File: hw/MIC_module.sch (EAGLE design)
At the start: 39 parts, among them J1 GROVE-4P-2.0-3470130P1, J2 GROVE-4P-2.0-3470130P1

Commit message: layout completed
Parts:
- removed J3: (no value), OPL-Connector:MICRO-SD-CARD-HOLDER-9P'MICROSD-9P'
- removed R6, R7, R9: 100k, rcl:R-EU_R0603
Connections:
- removed net SD_!CD: J3.CDN
- removed net SD_!CS: J3.CS, R9.1
- removed net SD_CLK: J3.SCLK
- removed net SD_MISO: J3.DO, R6.1
- removed net SD_MOSI: J3.DI, R7.1
- net +3V3: no longer J3.VDD, R6.2, R7.2, R9.2
- net GND: no longer J3.VSS
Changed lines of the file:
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@@
 <part name="C15" library="rcl" deviceset="C-EU" device="C0603" value="15p"/>
 <part name="GND27" library="supply1" deviceset="GND" device=""/>
-<part name="J3" library="OPL-Connector" deviceset="MICRO-SD-CARD-HOLDER-9P" device="'MICROSD-9P'"/>
-<part name="R6" library="rcl" deviceset="R-EU_" device="R0603" value="100k"/>
-<part name="R7" library="rcl" deviceset="R-EU_" device="R0603" value="100k"/>
-<part name="R9" library="rcl" deviceset="R-EU_" device="R0603" value="100k"/>
-<part name="+3V14" library="supply1" deviceset="+3V3" device=""/>
-<part name="GND28" library="supply1" deviceset="GND" device=""/>
 </parts>
 <sheets>
@@
 <instance part="C15" gate="G$1" x="195.58" y="149.86"/>
 <instance part="GND27" gate="1" x="195.58" y="142.24"/>
-<instance part="J3" gate="G$1" x="477.52" y="139.7"/>
-<instance part="R6" gate="G$1" x="452.12" y="157.48" rot="R90"/>
-<instance part="R7" gate="G$1" x="444.5" y="157.48" rot="R90"/>
-<instance part="R9" gate="G$1" x="436.88" y="157.48" rot="R90"/>
-<instance part="+3V14" gate="G$1" x="457.2" y="170.18"/>
-<instance part="GND28" gate="1" x="457.2" y="124.46"/>
 </instances>
 <busses>
@@
 <pinref part="C15" gate="G$1" pin="2"/>
 <pinref part="GND27" gate="1" pin="GND"/>
-</segment>
-<segment>
-<pinref part="J3" gate="G$1" pin="VSS"/>
-<wire x1="459.74" y1="137.16" x2="457.2" y2="137.16" width="0.1524" layer="91"/>
-<wire x1="457.2" y1="137.16" x2="457.2" y2="127" width="0.1524" layer="91"/>
-<pinref part="GND28" gate="1" pin="GND"/>
 </segment>
 </net>
@@
 <wire x1="180.34" y1="195.58" x2="180.34" y2="198.12" width="0.1524" layer="91"/>
 </segment>
-<segment>
-<pinref part="J3" gate="G$1" pin="VDD"/>
-<wire x1="459.74" y1="142.24" x2="457.2" y2="142.24" width="0.1524" layer="91"/>
-<wire x1="457.2" y1="142.24" x2="457.2" y2="165.1" width="0.1524" layer="91"/>
-<pinref part="+3V14" gate="G$1" pin="+3V3"/>
-<pinref part="R9" gate="G$1" pin="2"/>
-<wire x1="457.2" y1="165.1" x2="457.2" y2="167.64" width="0.1524" layer="91"/>
-<wire x1="457.2" y1="165.1" x2="452.12" y2="165.1" width="0.1524" layer="91"/>
-<wire x1="452.12" y1="165.1" x2="444.5" y2="165.1" width="0.1524" layer="91"/>
-<wire x1="444.5" y1="165.1" x2="436.88" y2="165.1" width="0.1524" layer="91"/>
-<wire x1="436.88" y1="165.1" x2="436.88" y2="162.56" width="0.1524" layer="91"/>
-<junction x="457.2" y="165.1"/>
-<pinref part="R7" gate="G$1" pin="2"/>
-<wire x1="444.5" y1="162.56" x2="444.5" y2="165.1" width="0.1524" layer="91"/>
-<junction x="444.5" y="165.1"/>
-<pinref part="R6" gate="G$1" pin="2"/>
-<wire x1="452.12" y1="162.56" x2="452.12" y2="165.1" width="0.1524" layer="91"/>
-<junction x="452.12" y="165.1"/>
-</segment>
 </net>
 <net name="JTMS" class="0">
@@
 </segment>
 </net>
-<net name="SD_!CS" class="0">
-<segment>
-<pinref part="J3" gate="G$1" pin="CS"/>
-<wire x1="459.74" y1="147.32" x2="436.88" y2="147.32" width="0.1524" layer="91"/>
-<pinref part="R9" gate="G$1" pin="1"/>
-<wire x1="436.88" y1="147.32" x2="431.8" y2="147.32" width="0.1524" layer="91"/>
-<wire x1="436.88" y1="152.4" x2="436.88" y2="147.32" width="0.1524" layer="91"/>
-<junction x="436.88" y="147.32"/>
-<label x="431.8" y="147.32" size="1.778" layer="95" rot="MR0"/>
-</segment>
-</net>
-<net name="SD_CLK" class="0">
-<segment>
-<pinref part="J3" gate="G$1" pin="SCLK"/>
-<wire x1="459.74" y1="139.7" x2="431.8" y2="139.7" width="0.1524" layer="91"/>
-<label x="431.8" y="139.7" size="1.778" layer="95" rot="MR0"/>
-</segment>
-</net>
-<net name="SD_MOSI" class="0">
-<segment>
-<pinref part="J3" gate="G$1" pin="DI"/>
-<wire x1="459.74" y1="144.78" x2="444.5" y2="144.78" width="0.1524" layer="91"/>
-<pinref part="R7" gate="G$1" pin="1"/>
-<wire x1="444.5" y1="144.78" x2="431.8" y2="144.78" width="0.1524" layer="91"/>
-<wire x1="444.5" y1="152.4" x2="444.5" y2="144.78" width="0.1524" layer="91"/>
-<junction x="444.5" y="144.78"/>
-<label x="431.8" y="144.78" size="1.778" layer="95" rot="MR0"/>
-</segment>
-</net>
-<net name="SD_MISO" class="0">
-<segment>
-<pinref part="J3" gate="G$1" pin="DO"/>
-<wire x1="459.74" y1="134.62" x2="452.12" y2="134.62" width="0.1524" layer="91"/>
-<pinref part="R6" gate="G$1" pin="1"/>
-<wire x1="452.12" y1="134.62" x2="431.8" y2="134.62" width="0.1524" layer="91"/>
-<wire x1="452.12" y1="152.4" x2="452.12" y2="134.62" width="0.1524" layer="91"/>
-<junction x="452.12" y="134.62"/>
-<label x="431.8" y="134.62" size="1.778" layer="95" rot="MR0"/>
-</segment>
-</net>
-<net name="SD_!CD" class="0">
-<segment>
-<pinref part="J3" gate="G$1" pin="CDN"/>
-<wire x1="459.74" y1="129.54" x2="431.8" y2="129.54" width="0.1524" layer="91"/>
-<label x="431.8" y="129.54" size="1.778" layer="95" rot="MR0"/>
-</segment>
-</net>

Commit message: layout in progress
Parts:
- removed U$6: STM32F303C, st:STM32F303C
- added C16, C18: 2u2, rcl:C-EUC0603
- added IC1: STM32F405RGT, micro-stm_v2:STM32F405RGT
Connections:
- removed net MIC_CLK_X2: U$6.PA5, U$6.PA6, U$6.PB13
- new net N$6: C16.2, IC1MCU.VCAP2
- new net N$9: C18.2, IC1MCU.VCAP1
- net +3V3: now also IC1MCU.VBAT, IC1MCU.VDDA, IC1PWR.VDD@1, IC1PWR.VDD@2, IC1PWR.VDD@3, IC1PWR.VDD@4; no longer U$6.VBAT, U$6.VDD_1, U$6.VDD_2, U$6.VDD_3, U$6.VDD_A
- net BOOT0: now also IC1MCU.BOOT0; no longer U$6.BOOT0
- net CAN_RX: now also IC1MCU.PB8; no longer U$6.PB8
- net CAN_TX: now also IC1MCU.PB9; no longer U$6.PB9
- net GND: now also C16.1, C18.1, IC1MCU.VSSA, IC1PWR.VSS@1, IC1PWR.VSS@2; no longer U$6.VSS_1, U$6.VSS_2, U$6.VSS_3, U$6.VSS_A
- net JTCK: now also IC1MCU.PA14; no longer U$6.PA14
- net JTDI: now also IC1MCU.PA15; no longer U$6.PA15
- net JTDO: now also IC1MCU.PB3; no longer U$6.PB3
- net JTMS: now also IC1MCU.PA13; no longer U$6.PA13
- net LED1: no longer U$6.PC13
- net MIC_CLK_UC: no longer U$6.PA2
- net MIC_PDM12: no longer U$6.PB15
- net MIC_PDM34: no longer U$6.PA7
- net NRST: now also IC1MCU.NRST; no longer U$6.NRST
- net OSC_IN: now also IC1MCU.OSC_IN; no longer U$6.PF0/OSC_IN

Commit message: added USB port
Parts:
- added J4: MICRO-USB-5P-340015001, OPL Eagle Library:MICRO-USB-5P-340015001
- added R11, R14: 22, rcl:R-EU_R0603
- added R6: 100k, rcl:R-EU_R0603
- added R8: 1k5, rcl:R-EU_R0603
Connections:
- new net N$3: J4.DM, R11.2
- new net N$32: J4.DP, R14.2, R8.2
- new net N$5: J4.ID, R6.2
- new net USB_N: IC1MCU.PA11, R11.1
- new net USB_P: IC1MCU.PA12, R14.1
- new net USB_VBUS: J4.VCC
- net +3V3: now also R8.1
- net GND: now also J4.GND@1, J4.GND@2, J4.GND@3, R6.1
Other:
- note added: "USB INTERFACE"
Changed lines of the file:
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@@
 <part name="GND32" library="supply1" deviceset="GND" device=""/>
 <part name="GND33" library="supply1" deviceset="GND" device=""/>
+<part name="GND38" library="supply1" deviceset="GND" device=""/>
+<part name="R11" library="rcl" deviceset="R-EU_" device="R0603" value="22"/>
+<part name="R14" library="rcl" deviceset="R-EU_" device="R0603" value="22"/>
+<part name="R6" library="rcl" deviceset="R-EU_" device="R0603" value="100k"/>
+<part name="GND35" library="supply1" deviceset="GND" device=""/>
+<part name="R8" library="rcl" deviceset="R-EU_" device="R0603" value="1k5"/>
+<part name="+3V15" library="supply1" deviceset="+3V3" device=""/>
+<part name="J4" library="OPL Eagle Library" deviceset="MICRO-USB-5P" device="-340015001"/>
 </parts>
 <sheets>
@@
 <wire x1="55.88" y1="5.08" x2="55.88" y2="43.18" width="0.1524" layer="94"/>
 <text x="58.42" y="38.1" size="2.54" layer="94">R2P BUS</text>
+<wire x1="152.4" y1="55.88" x2="213.36" y2="55.88" width="0.1524" layer="94"/>
+<wire x1="213.36" y1="55.88" x2="213.36" y2="5.08" width="0.1524" layer="94"/>
+<wire x1="213.36" y1="5.08" x2="152.4" y2="5.08" width="0.1524" layer="94"/>
+<wire x1="152.4" y1="5.08" x2="152.4" y2="55.88" width="0.1524" layer="94"/>
+<text x="154.94" y="50.8" size="2.54" layer="94">USB INTERFACE</text>
 </plain>
 <instances>
@@
 <instance part="GND32" gate="1" x="20.32" y="284.48"/>
 <instance part="GND33" gate="1" x="12.7" y="284.48"/>
+<instance part="GND38" gate="1" x="190.5" y="12.7"/>
+<instance part="R11" gate="G$1" x="172.72" y="33.02"/>
+<instance part="R14" gate="G$1" x="172.72" y="25.4"/>
+<instance part="R6" gate="G$1" x="182.88" y="20.32" rot="R90"/>
+<instance part="GND35" gate="1" x="182.88" y="12.7"/>
+<instance part="R8" gate="G$1" x="190.5" y="45.72" rot="R180"/>
+<instance part="+3V15" gate="G$1" x="198.12" y="53.34"/>
+<instance part="J4" gate="USB" x="200.66" y="27.94" rot="MR0"/>
 </instances>
 <busses>
@@
 <pinref part="C18" gate="G$1" pin="1"/>
 <pinref part="GND33" gate="1" pin="GND"/>
+</segment>
+<segment>
+<pinref part="GND38" gate="1" pin="GND"/>
+<wire x1="190.5" y1="15.24" x2="190.5" y2="22.86" width="0.1524" layer="91"/>
+<wire x1="200.66" y1="15.24" x2="198.12" y2="15.24" width="0.1524" layer="91"/>
+<wire x1="198.12" y1="15.24" x2="195.58" y2="15.24" width="0.1524" layer="91"/>
+<wire x1="195.58" y1="15.24" x2="193.04" y2="15.24" width="0.1524" layer="91"/>
+<wire x1="193.04" y1="15.24" x2="190.5" y2="15.24" width="0.1524" layer="91"/>
+<junction x="190.5" y="15.24"/>
+<pinref part="J4" gate="USB" pin="GND@1"/>
+<pinref part="J4" gate="USB" pin="GND@2"/>
+<wire x1="200.66" y1="15.24" x2="210.82" y2="15.24" width="0.1524" layer="91"/>
+<wire x1="210.82" y1="15.24" x2="210.82" y2="26.67" width="0.1524" layer="91"/>
+<pinref part="J4" gate="USB" pin="GND@3"/>
+<wire x1="210.82" y1="26.67" x2="210.82" y2="29.21" width="0.1524" layer="91"/>
+<junction x="210.82" y="26.67"/>
+</segment>
+<segment>
+<pinref part="R6" gate="G$1" pin="1"/>
+<pinref part="GND35" gate="1" pin="GND"/>
 </segment>
 </net>
@@
 <pinref part="+3V14" gate="G$1" pin="+3V3"/>
 </segment>
+<segment>
+<pinref part="R8" gate="G$1" pin="1"/>
+<wire x1="195.58" y1="45.72" x2="198.12" y2="45.72" width="0.1524" layer="91"/>
+<wire x1="198.12" y1="45.72" x2="198.12" y2="50.8" width="0.1524" layer="91"/>
+<pinref part="+3V15" gate="G$1" pin="+3V3"/>
+</segment>
 </net>
 <net name="JTMS" class="0">
@@
 </segment>
 </net>
+<net name="USB_VBUS" class="0">
+<segment>
+<wire x1="190.5" y1="33.02" x2="187.96" y2="33.02" width="0.1524" layer="91"/>
+<label x="170.18" y="40.64" size="1.778" layer="95" rot="MR0"/>
+<wire x1="187.96" y1="33.02" x2="187.96" y2="40.64" width="0.1524" layer="91"/>
+<wire x1="187.96" y1="40.64" x2="170.18" y2="40.64" width="0.1524" layer="91"/>
+<pinref part="J4" gate="USB" pin="VCC"/>
+</segment>
+</net>
+<net name="USB_N" class="0">
+<segment>
+<pinref part="R11" gate="G$1" pin="1"/>
+<wire x1="167.64" y1="33.02" x2="165.1" y2="33.02" width="0.1524" layer="91"/>
+<label x="165.1" y="33.02" size="1.778" layer="95" rot="MR0"/>
+</segment>
+<segment>
+<pinref part="IC1" gate="MCU" pin="PA11"/>
+<wire x1="68.58" y1="325.12" x2="71.12" y2="325.12" width="0.1524" layer="91"/>
+<label x="71.12" y="325.12" size="1.778" layer="95"/>
+</segment>
+</net>
+<net name="USB_P" class="0">
+<segment>
+<pinref part="R14" gate="G$1" pin="1"/>
+<wire x1="167.64" y1="25.4" x2="165.1" y2="25.4" width="0.1524" layer="91"/>
+<label x="165.1" y="25.4" size="1.778" layer="95" rot="MR0"/>
+</segment>
+<segment>
+<pinref part="IC1" gate="MCU" pin="PA12"/>
+<wire x1="68.58" y1="327.66" x2="71.12" y2="327.66" width="0.1524" layer="91"/>
+<label x="71.12" y="327.66" size="1.778" layer="95"/>
+</segment>
+</net>
+<net name="N$3" class="0">
+<segment>
+<wire x1="190.5" y1="30.48" x2="180.34" y2="30.48" width="0.1524" layer="91"/>
+<wire x1="180.34" y1="30.48" x2="180.34" y2="33.02" width="0.1524" layer="91"/>
+<pinref part="R11" gate="G$1" pin="2"/>
+<wire x1="180.34" y1="33.02" x2="177.8" y2="33.02" width="0.1524" layer="91"/>
+<pinref part="J4" gate="USB" pin="DM"/>
+</segment>
+</net>
+<net name="N$32" class="0">
+<segment>
+<wire x1="190.5" y1="27.94" x2="182.88" y2="27.94" width="0.1524" layer="91"/>
+<wire x1="182.88" y1="27.94" x2="180.34" y2="27.94" width="0.1524" layer="91"/>
+<wire x1="180.34" y1="27.94" x2="180.34" y2="25.4" width="0.1524" layer="91"/>
+<pinref part="R14" gate="G$1" pin="2"/>
+<wire x1="180.34" y1="25.4" x2="177.8" y2="25.4" width="0.1524" layer="91"/>
+<pinref part="R8" gate="G$1" pin="2"/>
+<wire x1="185.42" y1="45.72" x2="182.88" y2="45.72" width="0.1524" layer="91"/>
+<wire x1="182.88" y1="45.72" x2="182.88" y2="27.94" width="0.1524" layer="91"/>
+<junction x="182.88" y="27.94"/>
+<pinref part="J4" gate="USB" pin="DP"/>
+</segment>
+</net>
+<net name="N$5" class="0">
+<segment>
+<pinref part="R6" gate="G$1" pin="2"/>
+<wire x1="182.88" y1="25.4" x2="190.5" y2="25.4" width="0.1524" layer="91"/>
+<pinref part="J4" gate="USB" pin="ID"/>
+</segment>
+</net>

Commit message: layout completed
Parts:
- removed R3: 10k, rcl:R-EU_R0603
- added C19: 100n, rcl:C-EUC0603
- added X1: 53047-04, con-molex:53047-04
- added X2: 53047-06, con-molex:53047-06
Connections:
- removed net BOOT0: IC1MCU.BOOT0, R3.2
- new net I2C2_SCL: IC1MCU.PB10, X1-3.S
- new net I2C2_SDA: IC1MCU.PB11, X1-4.S
- new net I2S3_CK: IC1MCU.PC10, X2-4.S
- new net I2S3_MCK: IC1MCU.PC7, X2-5.S
- new net I2S3_SD: IC1MCU.PC12, X2-3.S
- new net I2S3_WS: IC1MCU.PA4, X2-6.S
- new net MIC_CLK_X2: IC1MCU.PA5, IC1MCU.PA6, IC1MCU.PB13
- net +3V3: now also C19.1, X1-1.S, X2-1.S
- net GND: now also C19.2, IC1MCU.BOOT0, LED1.C, X1-2.S, X2-2.S; no longer LED1.A, R3.1
- net LED1: now also IC1MCU.PB7
- net MIC_CLK_UC: now also IC1MCU.PB0
- net MIC_PDM12: now also IC1MCU.PB15
- net MIC_PDM34: now also IC1MCU.PA7
- net N$4: now also LED1.A; no longer LED1.C
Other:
- note added: "MIC ARRAY"
- moved on the sheet: C10, C11, C12, C13, C15, C16, C18, IC1, LED1, R2, R4, R5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

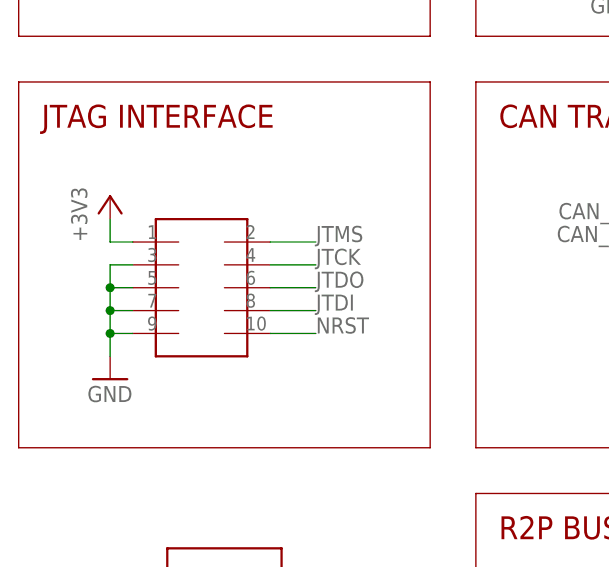
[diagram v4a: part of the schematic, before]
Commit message: Fixed silkscreen
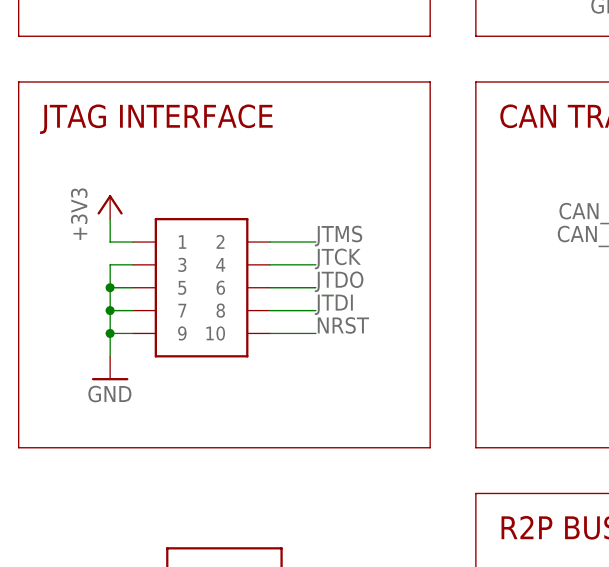
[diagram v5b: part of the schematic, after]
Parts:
- SOT1: device maxim:MAX3051EKA -> r2p_ic:MAX3051EKA
- U$3: device maxim:MAX17501 -> r2p_ic:MAX17501
- U$4: value FTSH-105TH -> JTAG-TH; device samtec:FTSH-105TH -> r2p_connector:JTAG-TH
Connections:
- net +3V3: now also U$4.1; no longer U$4.P$1
- net GND: now also U$4.3, U$4.5, U$4.7, U$4.9; no longer U$4.P$3, U$4.P$5, U$4.P$7, U$4.P$9
- net JTCK: now also U$4.4; no longer U$4.P$4
- net JTDI: now also U$4.8; no longer U$4.P$8
- net JTDO: now also U$4.6; no longer U$4.P$6
- net JTMS: now also U$4.2; no longer U$4.P$2
- net NRST: now also U$4.10; no longer U$4.P$10
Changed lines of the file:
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@@
 <part name="GND16" library="supply1" deviceset="GND" device=""/>
 <part name="GND17" library="supply1" deviceset="GND" device=""/>
-<part name="U$4" library="samtec" deviceset="FTSH-105" device="TH" value="FTSH-105TH"/>
+<part name="U$4" library="r2p_connector" deviceset="JTAG" device="-TH" value="JTAG-TH"/>
 <part name="+3V1" library="supply1" deviceset="+3V3" device=""/>
 <part name="GND19" library="supply1" deviceset="GND" device=""/>
@@
 <part name="GND2" library="supply" deviceset="GND" device=""/>
 <part name="GND3" library="supply" deviceset="GND" device=""/>
-<part name="U$3" library="maxim" deviceset="MAX17501" device=""/>
+<part name="U$3" library="r2p_ic" deviceset="MAX17501" device=""/>
 <part name="J1" library="OPL Eagle Library" deviceset="GROVE-4P-2.0" device="-3470130P1"/>
 <part name="+3V7" library="supply1" deviceset="+3V3" device=""/>
 <part name="FRAME1" library="frames" deviceset="DINA3_L" device=""/>
 <part name="GND13" library="supply" deviceset="GND" device=""/>
-<part name="SOT1" library="maxim" deviceset="MAX3051" device="EKA"/>
+<part name="SOT1" library="r2p_ic" deviceset="MAX3051" device="EKA"/>
 <part name="U$1" library="r2p_pcb" deviceset="PCB_25X45" device=""/>
 <part name="U$5" library="abracon" deviceset="ASD" device=""/>
@@
 <wire x1="17.78" y1="60.96" x2="15.24" y2="60.96" width="0.1524" layer="91"/>
 <wire x1="15.24" y1="60.96" x2="15.24" y2="58.42" width="0.1524" layer="91"/>
-<pinref part="U$4" gate="G$1" pin="P$9"/>
+<pinref part="U$4" gate="G$1" pin="9"/>
 <pinref part="GND19" gate="1" pin="GND"/>
-<pinref part="U$4" gate="G$1" pin="P$3"/>
+<pinref part="U$4" gate="G$1" pin="3"/>
 <wire x1="17.78" y1="68.58" x2="15.24" y2="68.58" width="0.1524" layer="91"/>
 <wire x1="15.24" y1="68.58" x2="15.24" y2="66.04" width="0.1524" layer="91"/>
 <junction x="15.24" y="60.96"/>
-<pinref part="U$4" gate="G$1" pin="P$5"/>
+<pinref part="U$4" gate="G$1" pin="5"/>
 <wire x1="15.24" y1="66.04" x2="15.24" y2="63.5" width="0.1524" layer="91"/>
 <wire x1="15.24" y1="63.5" x2="15.24" y2="60.96" width="0.1524" layer="91"/>
 <wire x1="17.78" y1="66.04" x2="15.24" y2="66.04" width="0.1524" layer="91"/>
 <junction x="15.24" y="66.04"/>
-<pinref part="U$4" gate="G$1" pin="P$7"/>
+<pinref part="U$4" gate="G$1" pin="7"/>
 <wire x1="17.78" y1="63.5" x2="15.24" y2="63.5" width="0.1524" layer="91"/>
 <junction x="15.24" y="63.5"/>
@@
 <wire x1="17.78" y1="71.12" x2="15.24" y2="71.12" width="0.1524" layer="91"/>
 <wire x1="15.24" y1="71.12" x2="15.24" y2="73.66" width="0.1524" layer="91"/>
-<pinref part="U$4" gate="G$1" pin="P$1"/>
+<pinref part="U$4" gate="G$1" pin="1"/>
 <pinref part="+3V1" gate="G$1" pin="+3V3"/>
 </segment>
@@
 <wire x1="33.02" y1="71.12" x2="38.1" y2="71.12" width="0.1524" layer="91"/>
 <label x="38.1" y="71.12" size="1.778" layer="95"/>
-<pinref part="U$4" gate="G$1" pin="P$2"/>
+<pinref part="U$4" gate="G$1" pin="2"/>
 </segment>
 </net>
@@
 <wire x1="33.02" y1="68.58" x2="38.1" y2="68.58" width="0.1524" layer="91"/>
 <label x="38.1" y="68.58" size="1.778" layer="95"/>
-<pinref part="U$4" gate="G$1" pin="P$4"/>
+<pinref part="U$4" gate="G$1" pin="4"/>
 </segment>
 </net>
@@
 <wire x1="33.02" y1="66.04" x2="38.1" y2="66.04" width="0.1524" layer="91"/>
 <label x="38.1" y="66.04" size="1.778" layer="95"/>
-<pinref part="U$4" gate="G$1" pin="P$6"/>
+<pinref part="U$4" gate="G$1" pin="6"/>
 </segment>
 </net>
@@
 <wire x1="33.02" y1="63.5" x2="38.1" y2="63.5" width="0.1524" layer="91"/>
 <label x="38.1" y="63.5" size="1.778" layer="95"/>
-<pinref part="U$4" gate="G$1" pin="P$8"/>
+<pinref part="U$4" gate="G$1" pin="8"/>
 </segment>
 </net>
@@
 <wire x1="33.02" y1="60.96" x2="38.1" y2="60.96" width="0.1524" layer="91"/>
 <label x="38.1" y="60.96" size="1.778" layer="95"/>
-<pinref part="U$4" gate="G$1" pin="P$10"/>
-</segment>
-</net>
+<pinref part="U$4" gate="G$1" pin="10"/>
+</segment>
+</net>
